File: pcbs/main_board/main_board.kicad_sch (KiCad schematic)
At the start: 11 parts, among them J3 LED strip, J4 Motor, U1 mini_esp32, U6 TPS22917LDBV

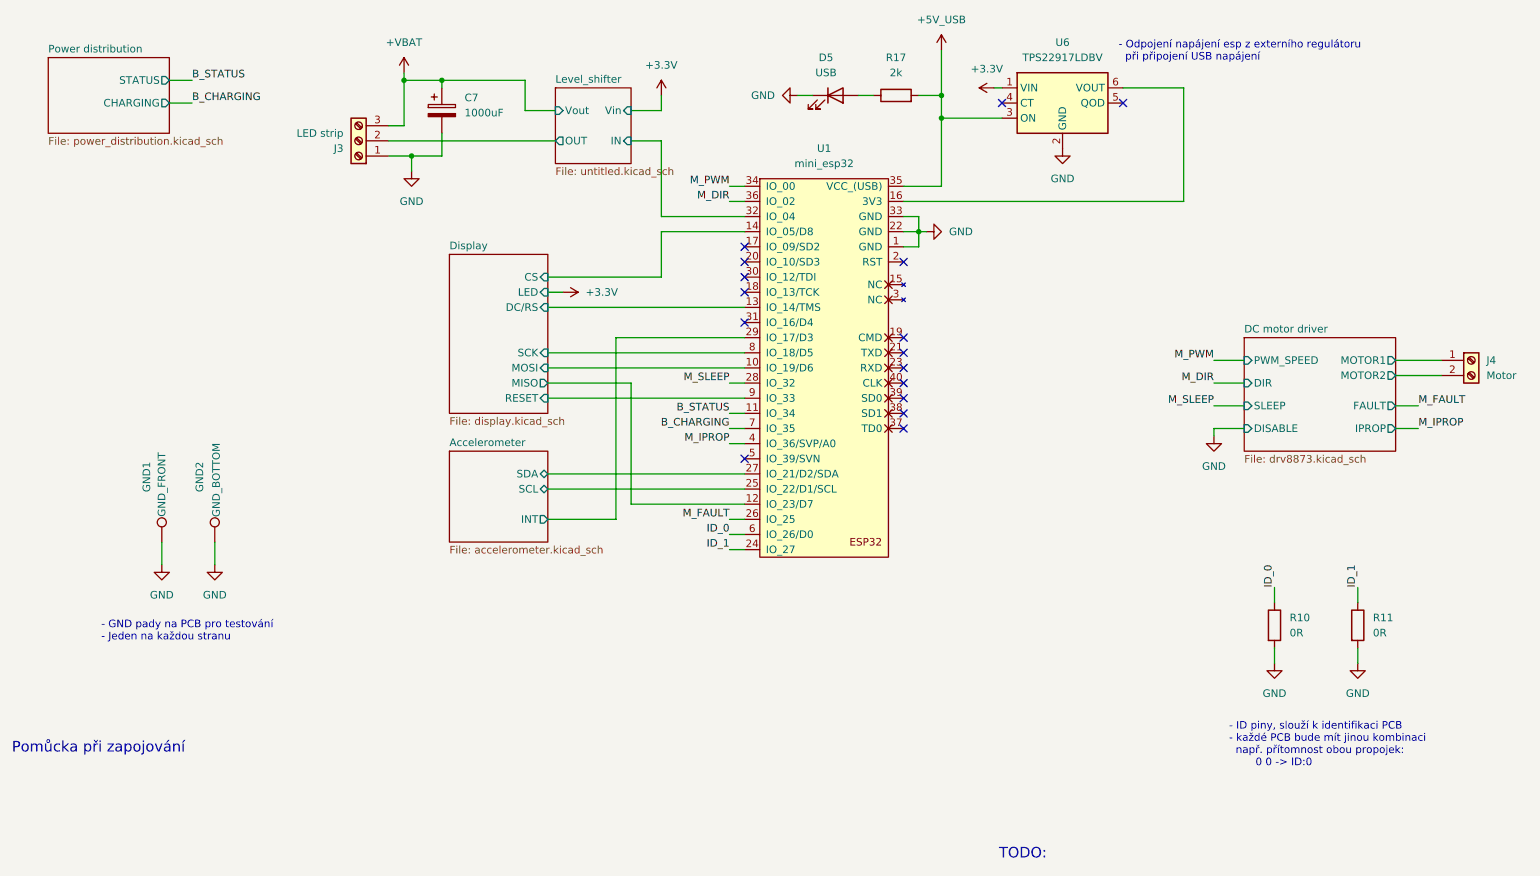
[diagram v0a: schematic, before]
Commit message: Add reverse polarity protection
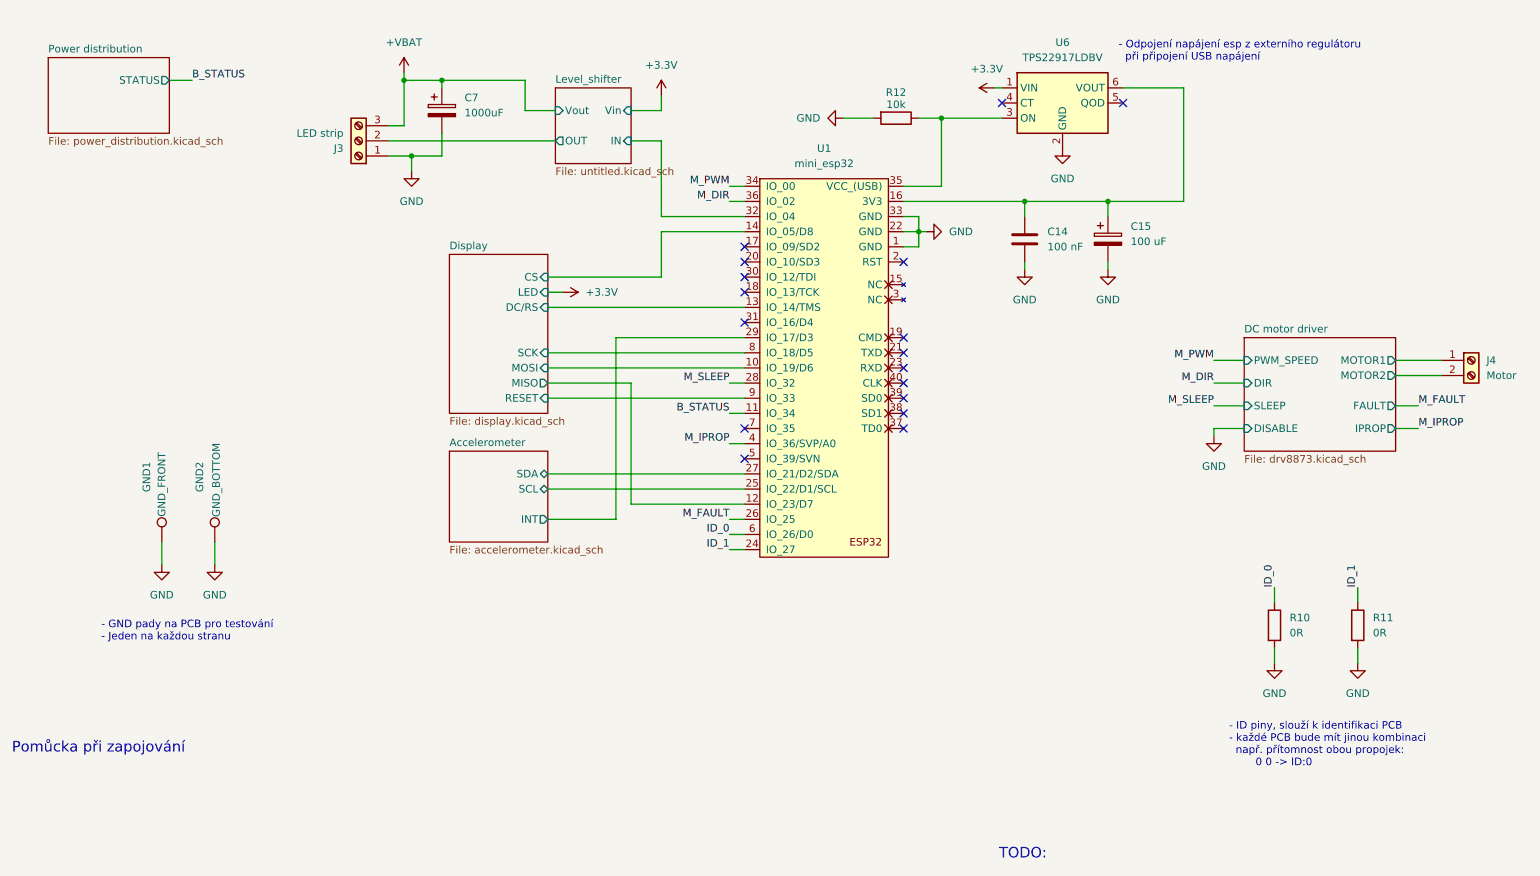
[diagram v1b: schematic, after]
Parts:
- removed D5: USB, LED_SMD:LED_0805_2012Metric_Pad1.15x1.40mm_HandSolder, symbol Device:LED
- removed R17: 2k, Resistor_SMD:R_0603_1608Metric_Pad0.98x0.95mm_HandSolder, symbol Device:R
- added C14: 100 nF, Capacitor_SMD:C_0603_1608Metric_Pad1.08x0.95mm_HandSolder, symbol Device:C
- added C15: 100 uF, Capacitor_Tantalum_SMD:CP_EIA-7343-40_Kemet-Y_HandSolder, symbol Device:C_Polarized
- added R12: 10k, Resistor_SMD:R_0603_1608Metric_Pad0.98x0.95mm_HandSolder, symbol Device:R
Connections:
- net GND: now also C14.2, C15.2, R12.2
- net at U1.16 (3V3), U6.6 (VOUT): now also C14.1, C15.1
- net +5V_USB: no longer names the net of U1.35 (VCC_(USB)), U6.3 (ON)
- net +5V_USB: now also R12.1
- net B_CHARGING: no longer names the net of U1.7 (IO_35)
- no-connect marks 16 -> 17
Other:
- sheet Power distribution ports: added none; removed CHARGING

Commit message: Components update
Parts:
- J3: Manufacturer Part Number S3B-XH-A-E(LF)(SN) -> S3B-XH-A-1 (LF)(SN); Supplier Mouser -> TME; Supplier Part Number 306-S3BXHAELFSN -> S3B-XH-A-1
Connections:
- net Display/MISO: no longer names the net of U1.12 (IO_23/D7)
- no-connect marks 17 -> 18
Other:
- sheet Display ports: added none; removed MISO
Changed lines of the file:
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@@
 	)
 	(no_connect
+		(at 135.89 95.25)
+	)
+	(no_connect
 		(at 162.56 69.85)
 	)
@@
 	(wire
 		(pts
-			(xy 116.84 74.93) (xy 116.84 95.25)
-		)
-		(stroke
-			(width 0)
-			(type default)
-		)
-	)
-	(wire
-		(pts
 			(xy 114.3 97.79) (xy 114.3 67.31)
 		)
@@
 	(wire
 		(pts
-			(xy 116.84 95.25) (xy 135.89 95.25)
-		)
-		(stroke
-			(width 0)
-			(type default)
-		)
-	)
-	(wire
-		(pts
 			(xy 78.74 24.13) (xy 78.74 31.75)
 		)
@@
 	(wire
 		(pts
-			(xy 102.87 74.93) (xy 116.84 74.93)
-		)
-		(stroke
-			(width 0)
-			(type default)
-		)
-	)
-	(wire
-		(pts
 			(xy 214.63 71.12) (xy 219.71 71.12)
 		)
@@
 			)
 		)
+		(property "Mouser number" ""
+			(at 189.23 27.94 0)
+			(effects
+				(font
+					(size 1.27 1.27)
+				)
+				(hide yes)
+			)
+		)
 		(pin "3"
 		)
@@
 			)
 		)
-		(property "Manufacturer Part Number" "S3B-XH-A-E(LF)(SN)"
+		(property "Manufacturer Part Number" "S3B-XH-A-1 (LF)(SN)"
 			(at 71.12 34.29 0)
 			(effects
@@
 			)
 		)
-		(property "Supplier" "Mouser"
+		(property "Supplier" "TME"
+			(at 71.12 34.29 0)
+			(effects
+				(font
+					(size 1.27 1.27)
+				)
+				(hide yes)
+			)
+		)
+		(property "Supplier Part Number" "S3B-XH-A-1"
 			(at 71.12 34.29 0)
 			(effects
@@
 			)
 		)
-		(property "Supplier Part Number" "306-S3BXHAELFSN"
+		(property "Mouser number" ""
 			(at 71.12 34.29 0)
 			(effects
@@
 			)
 		)
+		(property "Mouser number" ""
+			(at 46.99 101.6 90)
+			(effects
+				(font
+					(size 1.27 1.27)
+				)
+				(hide yes)
+			)
+		)
 		(pin "1"
 		)
@@
 			)
 		)
+		(property "Mouser number" ""
+			(at 38.1 101.6 90)
+			(effects
+				(font
+					(size 1.27 1.27)
+				)
+				(hide yes)
+			)
+		)
 		(pin "1"
 		)
@@
 			)
 		)
+		(property "Mouser number" ""
+			(at 224.79 115.57 0)
+			(effects
+				(font
+					(size 1.27 1.27)
+				)
+				(hide yes)
+			)
+		)
 		(pin "2"
 		)
@@
 			)
 		)
+		(property "Mouser number" ""
+			(at 257.81 71.12 0)
+			(effects
+				(font
+					(size 1.27 1.27)
+				)
+				(hide yes)
+			)
+		)
 		(pin "1"
 		)
@@
 			)
 		)
+		(property "Mouser number" ""
+			(at 238.76 115.57 0)
+			(effects
+				(font
+					(size 1.27 1.27)
+				)
+				(hide yes)
+			)
+		)
 		(pin "2"
 		)
@@
 			)
 		)
+		(property "Mouser number" ""
+			(at 196.85 50.8 0)
+			(effects
+				(font
+					(size 1.27 1.27)
+				)
+				(hide yes)
+			)
+		)
 		(pin "2"
 		)
@@
 			)
 		)
+		(property "Mouser number" ""
+			(at 85.09 29.21 0)
+			(effects
+				(font
+					(size 1.27 1.27)
+				)
+				(hide yes)
+			)
+		)
 		(pin "2"
 		)
@@
 			)
 		)
+		(property "Mouser number" ""
+			(at 148.59 39.37 0)
+			(effects
+				(font
+					(size 1.27 1.27)
+				)
+				(hide yes)
+			)
+		)
 		(pin "32"
 		)
@@
 			)
 		)
+		(property "Mouser number" ""
+			(at 161.29 30.48 90)
+			(effects
+				(font
+					(size 1.27 1.27)
+				)
+				(hide yes)
+			)
+		)
 		(pin "2"
 		)
@@
 			)
 		)
+		(property "Mouser number" ""
+			(at 182.88 50.8 0)
+			(effects
+				(font
+					(size 1.27 1.27)
+				)
+				(hide yes)
+			)
+		)
 		(pin "1"
 		)
@@
 			(effects
 				(font
-					(size 1.27 1.27)
-				)
-				(justify right)
-			)
-		)
-		(pin "MISO" output
-			(at 102.87 74.93 0)
-			(effects
-				(font

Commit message: Main board final update
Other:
- note removed: "TODO:"
- company: (none) -> Brno Mars Rover
- title: (none) -> Main board - MyMachine LED cap
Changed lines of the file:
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@@
 	(generator_version "9.0")
 	(paper "A4")
-	(text "TODO:\n\n"
-		(exclude_from_sim no)
-		(at 178.562 152.908 0)
-		(effects
-			(font
-				(size 1.778 1.778)
-			)
-			(justify left top)
-		)
+	(title_block
+		(title "Main board - MyMachine LED cap")
+		(date "2026-01-20")
+		(company "Brno Mars Rover")
 	)
 	(text "Pomůcka při zapojování"

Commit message: Fix bom errors - main board
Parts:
- C14: Supplier Part Number 603-CC603KRX7R9BB103 -> 80-C0603C104M5R
- R12: Manufacturer Part Number CRCW0603910KFKEAHP -> CRCW060310K0FKEI; Supplier Part Number 71-CRCW0603910KFKEAH -> 71-CRCW060310K0FKEI
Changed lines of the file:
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@@
 			)
 		)
-		(property "Manufacturer Part Number" "CRCW0603910KFKEAHP"
+		(property "Manufacturer Part Number" "CRCW060310K0FKEI"
 			(at 161.29 30.48 90)
 			(effects
@@
 			)
 		)
-		(property "Supplier Part Number" "71-CRCW0603910KFKEAH"
+		(property "Supplier Part Number" "71-CRCW060310K0FKEI"
 			(at 161.29 30.48 90)
 			(effects
@@
 			)
 		)
-		(property "Supplier Part Number" "603-CC603KRX7R9BB103"
+		(property "Supplier Part Number" "80-C0603C104M5R"
 			(at 182.88 50.8 0)
 			(effects
